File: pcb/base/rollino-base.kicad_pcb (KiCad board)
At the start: 2 copper layers, 64 x 76.5 mm, 11 parts, among them J1 FH12-6S-0.5SH, J2 FH12-6S-0.5SH, U1 XIAO nRF52840

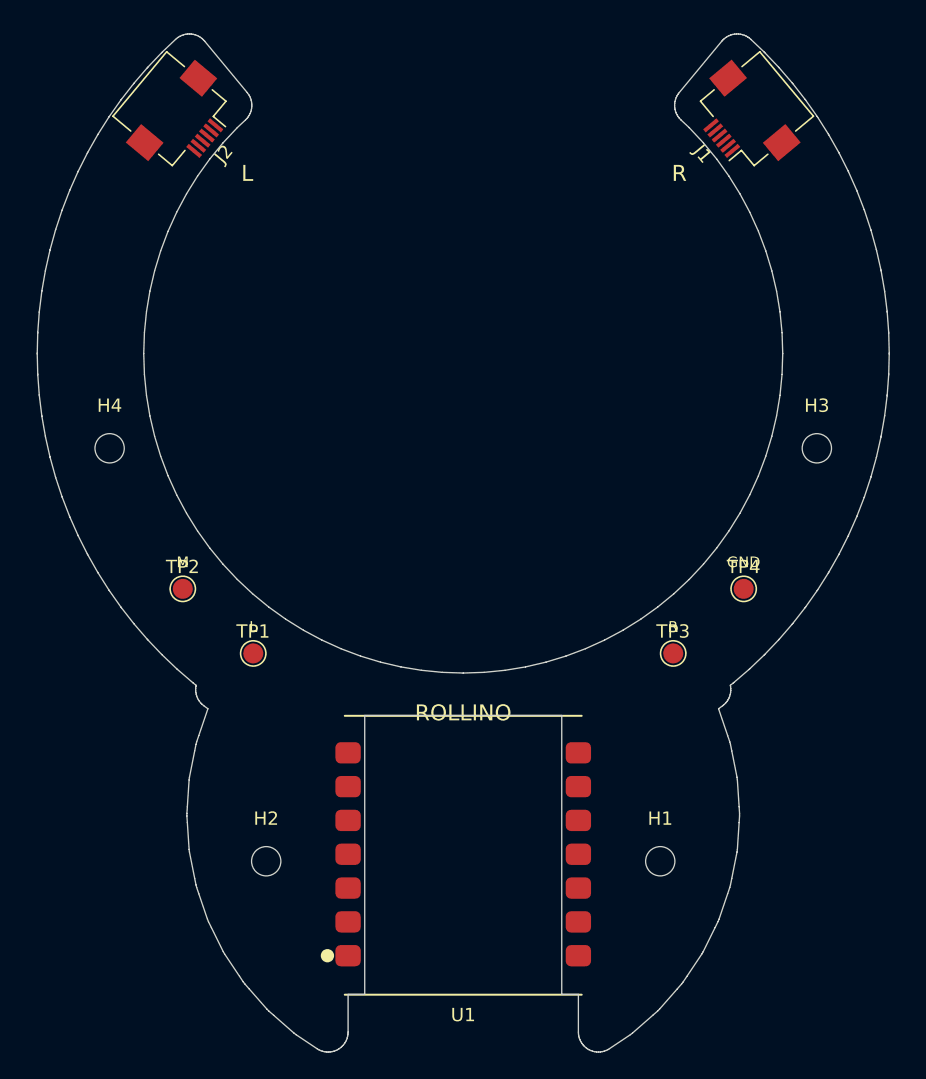
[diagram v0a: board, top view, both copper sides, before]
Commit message: Route both PCBs, copper logo, 3D renders of the boards
pcb/gen/route.py has Freerouting route every net (edge and logo keep-outs,
retrying strategies until nothing is left unconnected) and pours GND;
pcb/gen/render_pcbs.sh renders both boards in Blender from KiCad's VRML,
with generated models for the upside-down XIAO and the PMW3610 + lens. The
ROLLINO logo is now bare copper on the back of the band instead of
silkscreen cut by the XIAO's cutout. Connector mounting tabs go to GND;
mounting holes have symbols; the band is 0.5 mm wider for the connectors'
escape routes.

Co-Authored-By: Claude Opus 5.5 <noreply@anthropic.com>
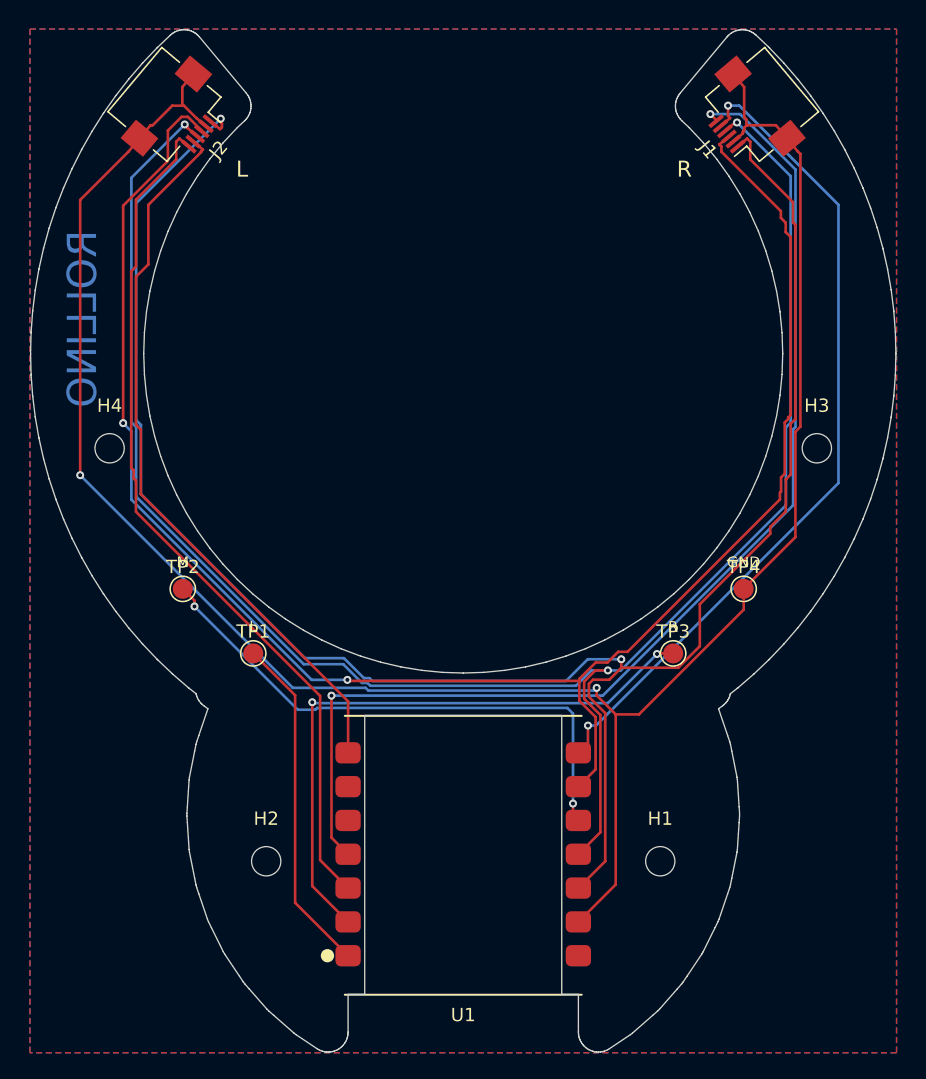
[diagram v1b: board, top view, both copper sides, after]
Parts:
- moved J1 0.50 mm to (171.2, 82.3), turned to 130 degrees
- moved J2 0.50 mm to (128.8, 82.3), turned to -130 degrees
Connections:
- net BTN_L renamed /BTN_L
- net BTN_M renamed /BTN_M
- net BTN_R renamed /BTN_R
- net MOTION_L renamed /MOTION_L
- net MOTION_R renamed /MOTION_R
- net NCS_L renamed /NCS_L
- net NCS_R renamed /NCS_R
- net SCLK renamed /SCLK
- net SDIO renamed /SDIO
- J1 pad MP: (no net) -> GND
- J2 pad MP: (no net) -> GND
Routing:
- net GND: track 0.00 -> 161.2 mm, vias 0 -> 2
- net +3V3: track 0.00 -> 145.8 mm, vias 0 -> 2
- net /SDIO: track 0.00 -> 139.4 mm, vias 0 -> 3
- net /SCLK: track 0.00 -> 132.1 mm, vias 0 -> 2
- net /MOTION_R: track 0.00 -> 87.2 mm, vias 0 -> 2
- net /MOTION_L: track 0.00 -> 65.5 mm
- net /NCS_R: track 0.00 -> 62.9 mm, vias 0 -> 2
- net /NCS_L: track 0.00 -> 54.9 mm
- net /BTN_R: track 0.00 -> 46.3 mm, vias 0 -> 2
- net /BTN_M: track 0.00 -> 41.8 mm, vias 0 -> 2
- net /BTN_L: track 0.00 -> 25.7 mm
- added copper zone on B.Cu, net GND
- added copper zone on F.Cu, net GND
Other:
- board size 64 x 76.5 mm -> 65 x 76.8 mm

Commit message: Sensor FPC mouth at the board edge, roomier ribbon channel, clean DRC
The sensor board's FH12 now faces off its up-slope edge, so the ribbon can
be pushed in and latched before the board goes into its pod; the pod has
room for the ribbon's U-turn back over the connector. The ribbon's channel
down through the pod is wider and deeper: part="fpc_check" sweeps a 1.5 mm
thick stand-in along its path and must come out empty, so the free end can
be fed through from either end. Ribbons are 40 mm.

Both boards pass DRC with nothing reported, warnings included: the
regulator moves clear of the sensor's courtyard (its EN tied to VIN by a
locked track route.py keeps), unconnected pins get the schematic's nets,
crowded references go to the fab layer. A small copper ROLLINO logo on the
sensor board's back.

The exploded view is rendered in Blender with KiCad's 3D models of the
boards (case/render_exploded.sh); case/render_previews.sh redoes the
OpenSCAD previews, render_pcbs.sh the layout images and schematic PDFs.

Co-Authored-By: Claude Opus 5.5 <noreply@anthropic.com>
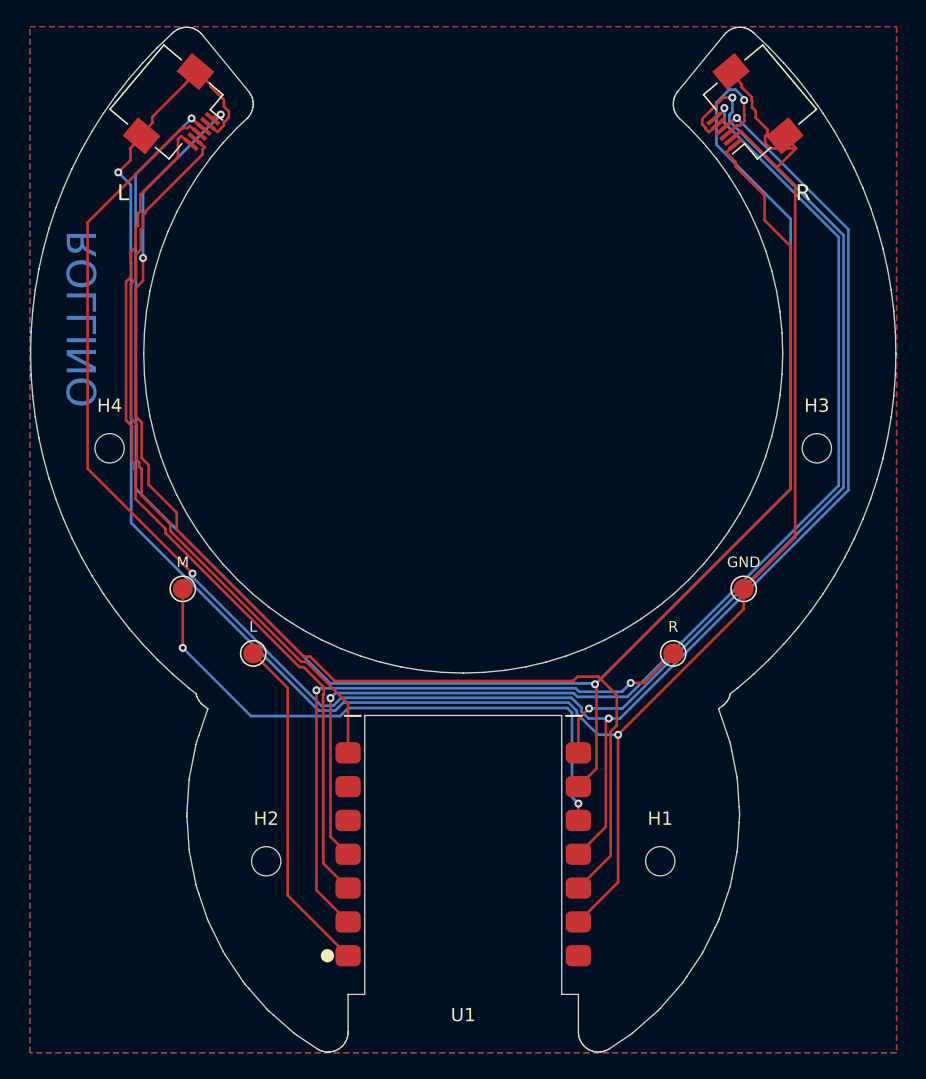
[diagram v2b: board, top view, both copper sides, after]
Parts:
- moved J1 0.24 mm to (171.1, 82.1)
- moved J2 0.24 mm to (128.9, 82.1)
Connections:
- U1 pad 14: (no net) -> unconnected-(U1-5V-Pad14)
- U1 pad 5: (no net) -> unconnected-(U1-D4/SDA-Pad5)
- U1 pad 6: (no net) -> unconnected-(U1-D5/SCL-Pad6)
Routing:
- net /SDIO: track 139.4 -> 146.9 mm
- net +3V3: track 145.8 -> 138.4 mm
- net GND: track 161.2 -> 168.4 mm
- net /SCLK: track 132.1 -> 137.9 mm, vias 2 -> 3
- net /NCS_R: track 62.9 -> 67.7 mm
- net /MOTION_R: track 87.2 -> 90.4 mm
- net /BTN_M: track 41.8 -> 44.5 mm
- net /MOTION_L: track 65.5 -> 66.3 mm
- net /NCS_L: track 54.9 -> 55.7 mm
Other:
- board size 65 x 76.8 mm -> 65 x 77 mm

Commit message: Shorter base band for a stock 50 mm FFC, parts list, FPC pin order fix
The base board's band now ends at about 110 degrees, with the FPC
connectors lying along it; each ribbon creases flat under its sensor pod
and runs along a channel in the case's underside, held by the cover.
The model solves the crease position from fpc_len = 50 (type B cable).
Connector pins are numbered from the ribbon's path so each signal meets
itself (the flipped sensor connector had reversed them).
Adds parts.md, the parts to order.

Co-Authored-By: Claude Opus 5.5 <noreply@anthropic.com>
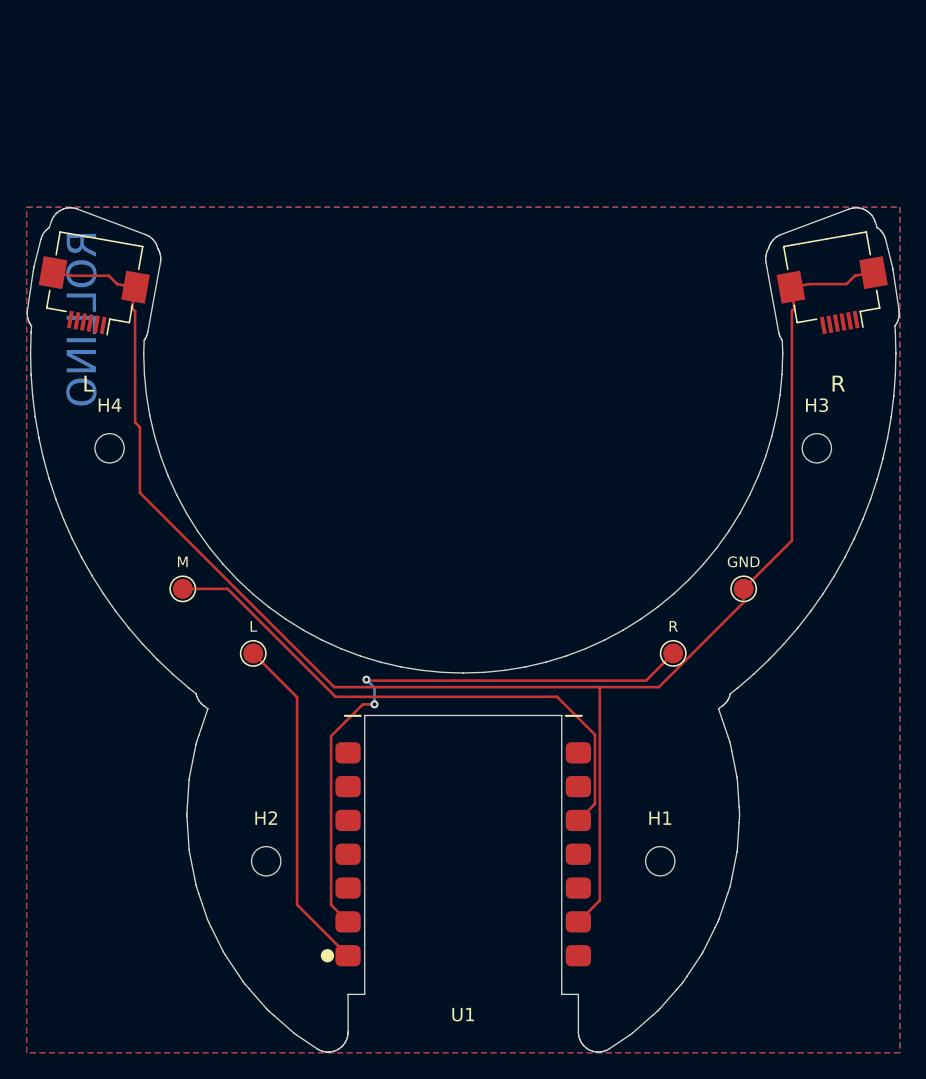
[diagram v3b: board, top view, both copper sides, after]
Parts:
- moved J2 15.4 mm to (122.0, 95.8), turned to 170 degrees
- moved J1 15.4 mm to (178.0, 95.8), turned to -170 degrees
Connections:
- J1 pad 1: +3V3 -> /MOTION_R
- J1 pad 2: GND -> /NCS_R
- J1 pad 3: /SCLK -> /SDIO
- J1 pad 4: /SDIO -> /SCLK
- J1 pad 5: /NCS_R -> GND
- J1 pad 6: /MOTION_R -> +3V3
- J2 pad 1: +3V3 -> /MOTION_L
- J2 pad 2: GND -> /NCS_L
- J2 pad 3: /SCLK -> /SDIO
- J2 pad 4: /SDIO -> /SCLK
- J2 pad 5: /NCS_L -> GND
- J2 pad 6: /MOTION_L -> +3V3
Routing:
- net /SDIO: track 146.9 -> 0.00 mm, vias 3 -> 0
- net +3V3: track 138.4 -> 0.00 mm, vias 2 -> 0
- net /SCLK: track 137.9 -> 0.00 mm, vias 3 -> 0
- net /MOTION_R: track 90.4 -> 0.00 mm, vias 2 -> 0
- net /NCS_R: track 67.7 -> 0.00 mm, vias 2 -> 0
- net /MOTION_L: track 66.3 -> 0.00 mm
- net /NCS_L: track 55.7 -> 0.00 mm
- net GND: track 168.4 -> 126.3 mm, vias 2 -> 0
- net /BTN_M: track 44.5 -> 42.5 mm, vias 2 -> 0
- net /BTN_R: track 46.5 -> 44.8 mm
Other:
- board size 65 x 77 mm -> 65.5 x 63.4 mm

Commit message: Route the base board again, clear the antenna, sensor decoupling by the pins
The base board had come out with nothing routed to its FPC connectors:
Freerouting can't start a track from their pads at this angle. generate.py
now lays a stub out of each pad and route.py has Freerouting join those;
route.py only saves a board that is whole and that KiCad's DRC has nothing
to report on, trying its other strategies otherwise.

Base board: no pour by the XIAO's antenna (the strip between the notch and
the ball's hole), the supply laid across that strip on the back, each
connector's grounds with their own vias to the pours, the pours stitched
together. The bus moves to D4/D5 (the XIAO's only pins that aren't kept
for low frequencies), the right sensor's MOTION to D8, and the buttons are
left, middle, right on D0, D1, D9, so each side's lines stay on its side.

Sensor board: each capacitor by the pin it serves on a short wide track
(PixArt's rule for CP, CN and VCP), the regulator's output capacitor
against it, a ground rail with vias from pin 11, 1.8 V round the lens
cutout on the back, test pads for 1.8 V and GND. Same parts.

Firmware: the new pins, the sensors' angles as the case model has them
now (elevation -22), full transmit power. Case: a hole in the cover under
the XIAO's reset button. The XIAO's 3D model on the base board was a
mirror image.

Co-Authored-By: Claude Opus 5.5 <noreply@anthropic.com>
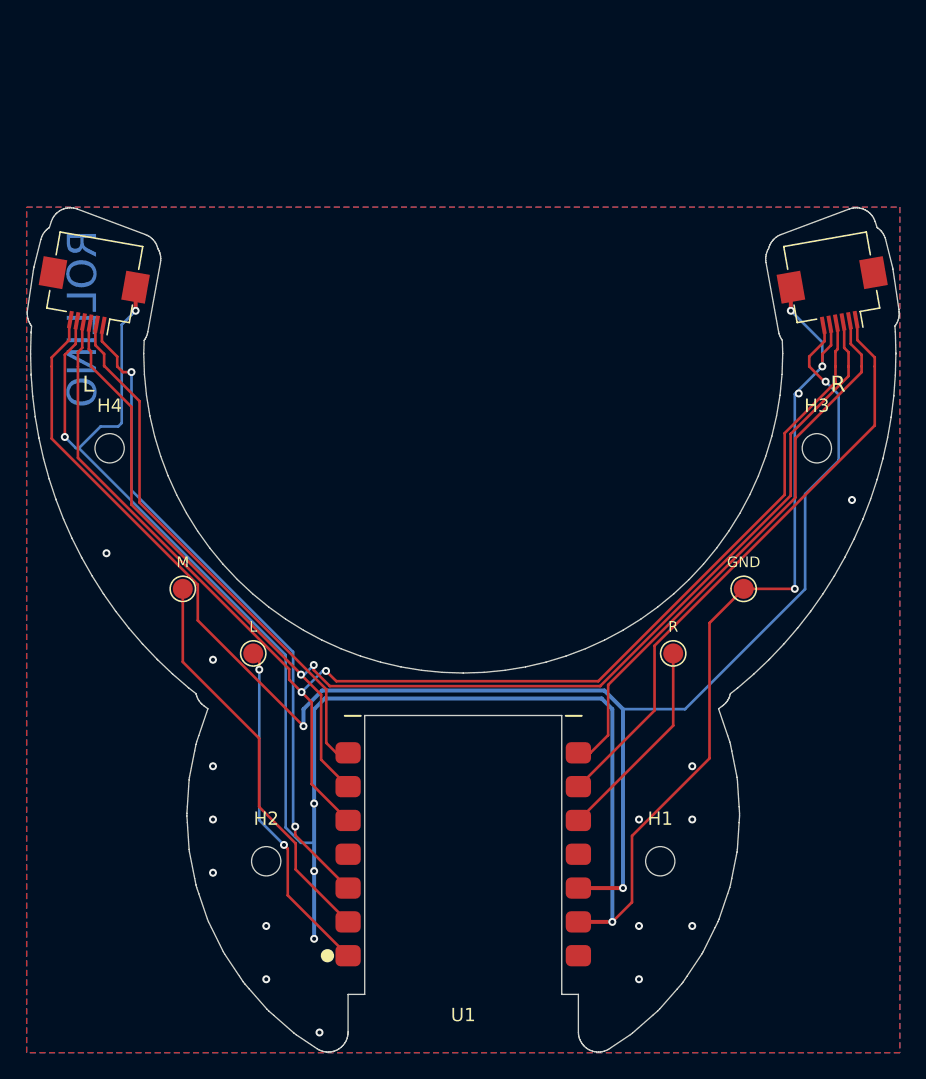
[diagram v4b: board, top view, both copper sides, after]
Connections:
- U1 pad 10: /BTN_M -> /BTN_R
- U1 pad 11: /SDIO -> unconnected-(U1-D10/MOSI-Pad11)
- U1 pad 2: /BTN_R -> /BTN_M
- U1 pad 4: /MOTION_R -> unconnected-(U1-D3-Pad4)
- U1 pad 5: unconnected-(U1-D4/SDA-Pad5) -> /SCLK
- U1 pad 6: unconnected-(U1-D5/SCL-Pad6) -> /SDIO
- U1 pad 9: /SCLK -> /MOTION_R
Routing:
- net +3V3: track 0.00 -> 121.3 mm, vias 0 -> 3
- net /SCLK: track 0.00 -> 102.7 mm, vias 0 -> 2
- net /SDIO: track 0.00 -> 100.9 mm, vias 0 -> 2
- net GND: track 126.3 -> 181.5 mm, vias 0 -> 25
- net /MOTION_L: track 0.00 -> 49.9 mm, vias 0 -> 2
- net /MOTION_R: track 0.00 -> 44.4 mm
- net /NCS_R: track 0.00 -> 41.7 mm
- net /NCS_L: track 0.00 -> 40.2 mm
- net /BTN_R: track 44.8 -> 15.5 mm, vias 2 -> 0
- net /BTN_M: track 42.5 -> 30.2 mm
- net /BTN_L: vias 0 -> 2
